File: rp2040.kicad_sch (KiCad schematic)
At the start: 25 parts, among them J1 Conn_01x06, J10 Conn_01x02, U6 RP2040, Y1 12.0MHz

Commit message: TT 4+ pre-route alpha schem and layout reset
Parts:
- C? (x2): footprint Capacitor_SMD:C_0402_1005Metric -> Capacitor_SMD:C_0603_1608Metric; MPN 1uF 0402 -> 1uF 0603
- C?: JLC C85864 -> (none); MPN CL10B104KB8NNND -> 100n 10% 25V XR 0603
- R11: footprint Resistor_SMD:R_0402_1005Metric -> Resistor_SMD:R_0603_1608Metric; MPN 10k 0402 -> 10k 0603

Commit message: reassignments, new dual-purpose pmod/iohead, floorplan
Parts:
- C?: footprint Capacitor_SMD:C_0603_1608Metric -> Capacitor_SMD:C_0402_1005Metric
- J1: footprint Connector_PinHeader_2.54mm:PinHeader_1x06_P2.54mm_Vertical -> Connector_PinHeader_2.54mm:PinHeader_1x06_P2.54mm_Vertical_SMD_Pin1Right
- R11, R? (x6): footprint Resistor_SMD:R_0603_1608Metric -> Resistor_SMD:R_0402_1005Metric
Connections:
- net +3.3V is gone; now on net QSPI_SD1: J1.5 (Pin_5)
- net BOOT_MODE: now also J1.2 (Pin_2); no longer J1.1 (Pin_1)
- net QSPI_CLK: now also J1.3 (Pin_3); no longer J1.2 (Pin_2)
- net QSPI_SD0: now also J1.4 (Pin_4); no longer J1.3 (Pin_3)
- net QSPI_SD1: no longer J1.4 (Pin_4)
- new net +3V3: J1.1 (Pin_1)
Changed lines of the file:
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@@
     (stroke (width 0) (type default))
   )
-  (wire (pts (xy 25.4 78.74) (xy 30.48 78.74))
+  (wire (pts (xy 25.4 78.74) (xy 35.56 78.74))
     (stroke (width 0) (type default))
   )
@@
     (effects (font (size 1 1)) (justify left bottom))
   )
-  (label "QSPI_SS" (at 35.56 68.58 180) (fields_autoplaced)
+  (label "QSPI_SS" (at 35.56 71.12 180) (fields_autoplaced)
     (effects (font (size 1.27 1.27)) (justify right bottom))
   )
@@
     (effects (font (size 1.27 1.27)) (justify right bottom))
   )
-  (label "QSPI_SD1" (at 35.56 76.2 180) (fields_autoplaced)
+  (label "QSPI_SD1" (at 35.56 78.74 180) (fields_autoplaced)
     (effects (font (size 1.27 1.27)) (justify right bottom))
   )
@@
     (effects (font (size 1.27 1.27)) (justify left bottom))
   )
-  (label "QSPI_SD0" (at 35.56 73.66 180) (fields_autoplaced)
+  (label "QSPI_SD0" (at 35.56 76.2 180) (fields_autoplaced)
     (effects (font (size 1.27 1.27)) (justify right bottom))
   )
@@
     (effects (font (size 1.27 1.27)) (justify right bottom))
   )
-  (label "QSPI_CLK" (at 35.56 71.12 180) (fields_autoplaced)
+  (label "QSPI_CLK" (at 35.56 73.66 180) (fields_autoplaced)
     (effects (font (size 1.27 1.27)) (justify right bottom))
   )
@@
       (effects (font (size 1.27 1.27)) (justify left))
     )
-    (property "Footprint" "Resistor_SMD:R_0603_1608Metric" (at 80.01 167.64 0)
+    (property "Footprint" "Resistor_SMD:R_0402_1005Metric" (at 80.01 167.64 0)
       (effects (font (size 1.27 1.27)) hide)
     )
@@
       (effects (font (size 1.27 1.27)) (justify left))
     )
-    (property "Footprint" "Resistor_SMD:R_0603_1608Metric" (at 73.66 109.22 0)
+    (property "Footprint" "Resistor_SMD:R_0402_1005Metric" (at 73.66 109.22 0)
       (effects (font (size 1.27 1.27)) hide)
     )
@@
       (effects (font (size 1.27 1.27)) (justify left))
     )
-    (property "Footprint" "Resistor_SMD:R_0603_1608Metric" (at 25.4 170.18 0)
+    (property "Footprint" "Resistor_SMD:R_0402_1005Metric" (at 25.4 170.18 0)
       (effects (font (size 1.27 1.27)) hide)
     )
@@
       (effects (font (size 1.27 1.27)) hide)
     )
-    (property "Footprint" "Connector_PinHeader_2.54mm:PinHeader_1x06_P2.54mm_Vertical" (at 20.32 73.66 0)
+    (property "Footprint" "Connector_PinHeader_2.54mm:PinHeader_1x06_P2.54mm_Vertical_SMD_Pin1Right" (at 20.32 73.66 0)
       (effects (font (size 1.27 1.27)) hide)
     )
@@
       (effects (font (size 1.27 1.27)) (justify right))
     )
-    (property "Footprint" "Resistor_SMD:R_0603_1608Metric" (at 73.66 48.26 0)
+    (property "Footprint" "Resistor_SMD:R_0402_1005Metric" (at 73.66 48.26 0)
       (effects (font (size 1.27 1.27)) hide)
     )
@@
       (effects (font (size 1.27 1.27)) (justify left))
     )
-    (property "Footprint" "Resistor_SMD:R_0603_1608Metric" (at 73.66 167.64 0)
+    (property "Footprint" "Resistor_SMD:R_0402_1005Metric" (at 73.66 167.64 0)
       (effects (font (size 1.27 1.27)) hide)
     )
@@
     )
   )
-  (symbol (lib_id "power:+3.3V") (at 30.48 78.74 270) (mirror x) (unit 1)
+  (symbol (lib_id "power:+3V3") (at 35.56 68.58 270) (mirror x) (unit 1)
     (in_bom yes) (on_board yes) (dnp no) (fields_autoplaced)
-    (property "Reference" "#PWR09" (at 26.67 78.74 0)
+    (property "Reference" "#PWR09" (at 31.75 68.58 0)
       (effects (font (size 1.27 1.27)) hide)
     )
-    (property "Value" "+3.3V" (at 33.655 78.74 90)
+    (property "Value" "+3V3" (at 38.735 68.58 90)
       (effects (font (size 1.27 1.27)) (justify left))
     )
-    (property "Footprint" "" (at 30.48 78.74 0)
+    (property "Footprint" "" (at 35.56 68.58 0)
       (effects (font (size 1.27 1.27)) hide)
     )
-    (property "Datasheet" "" (at 30.48 78.74 0)
+    (property "Datasheet" "" (at 35.56 68.58 0)
       (effects (font (size 1.27 1.27)) hide)
     )
@@
       (effects (font (size 1.27 1.27)) (justify left))
     )
-    (property "Footprint" "Resistor_SMD:R_0603_1608Metric" (at 86.36 167.64 0)
+    (property "Footprint" "Resistor_SMD:R_0402_1005Metric" (at 86.36 167.64 0)
       (effects (font (size 1.27 1.27)) hide)
     )
@@
       (effects (font (size 1.27 1.27)))
     )
-    (property "Footprint" "Capacitor_SMD:C_0603_1608Metric" (at 57.15 167.64 0)
+    (property "Footprint" "Capacitor_SMD:C_0402_1005Metric" (at 57.15 167.64 0)
       (effects (font (size 1.27 1.27)) hide)
     )
@@
       (effects (font (size 1.27 1.27)) (justify left))
     )
-    (property "Footprint" "Resistor_SMD:R_0603_1608Metric" (at 67.31 167.64 0)
+    (property "Footprint" "Resistor_SMD:R_0402_1005Metric" (at 67.31 167.64 0)
       (effects (font (size 1.27 1.27)) hide)
     )

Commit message: TT04 new breakout pre-rework
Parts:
- C?: Characteristics (none) -> 6pF 10% 50V XR 0402; MPN 6pF 10% 50V XR 0402 -> CC0402BRNPO9BN6R0
- C? (x8): Characteristics (none) -> 100n 10% 25V XR 0402; MPN 100nF 0402 -> CL05A104KA5NNNC; MPN_ALT (none) -> GRM155R71E104KE14J
- C? (x2): Characteristics (none) -> 1u 10V XR 0603; MPN 1uF 0603 -> CL10A105KA8NNNC; MPN_ALT (none) -> C0603C105K4RAC7411
- C?: Characteristics (none) -> 6pF 10% 50V XR 0402; MPN 6pF 10% 50V XR 0402 -> CC0402BRNPO9BN6R0; MPN_ALT (none) -> 0402N6R0D500CT
- C?: Characteristics (none) -> 100n 10% 25V XR 0402; MPN 100n 10% 25V XR 0603 -> CL05A104KA5NNNC; MPN_ALT (none) -> GRM155R71E104KE14J
- R11: Characteristics (none) -> 10k 0402; MPN 10k 0603 -> RC0402FR-0710KL; MPN_ALT (none) -> WR04X1002FTL
- R? (x5): Characteristics (none) -> 10k 0402; MPN (none) -> RC0402FR-0710KL; MPN_ALT (none) -> WR04X1002FTL
- R?: Characteristics (none) -> 1k 0402; MPN (none) -> CR0402-FX-1001GLF; MPN_ALT (none) -> WR04X1001FTL
- U6: DigikeyPN (none) -> 2648-SC0914(13)CT-ND; MPN (none) -> SC0914(13)
- U?: DigikeyPN (none) -> W25Q32JVSSIQ-ND
- Y1: DigikeyPN (none) -> 1923-830108206909DKR-ND

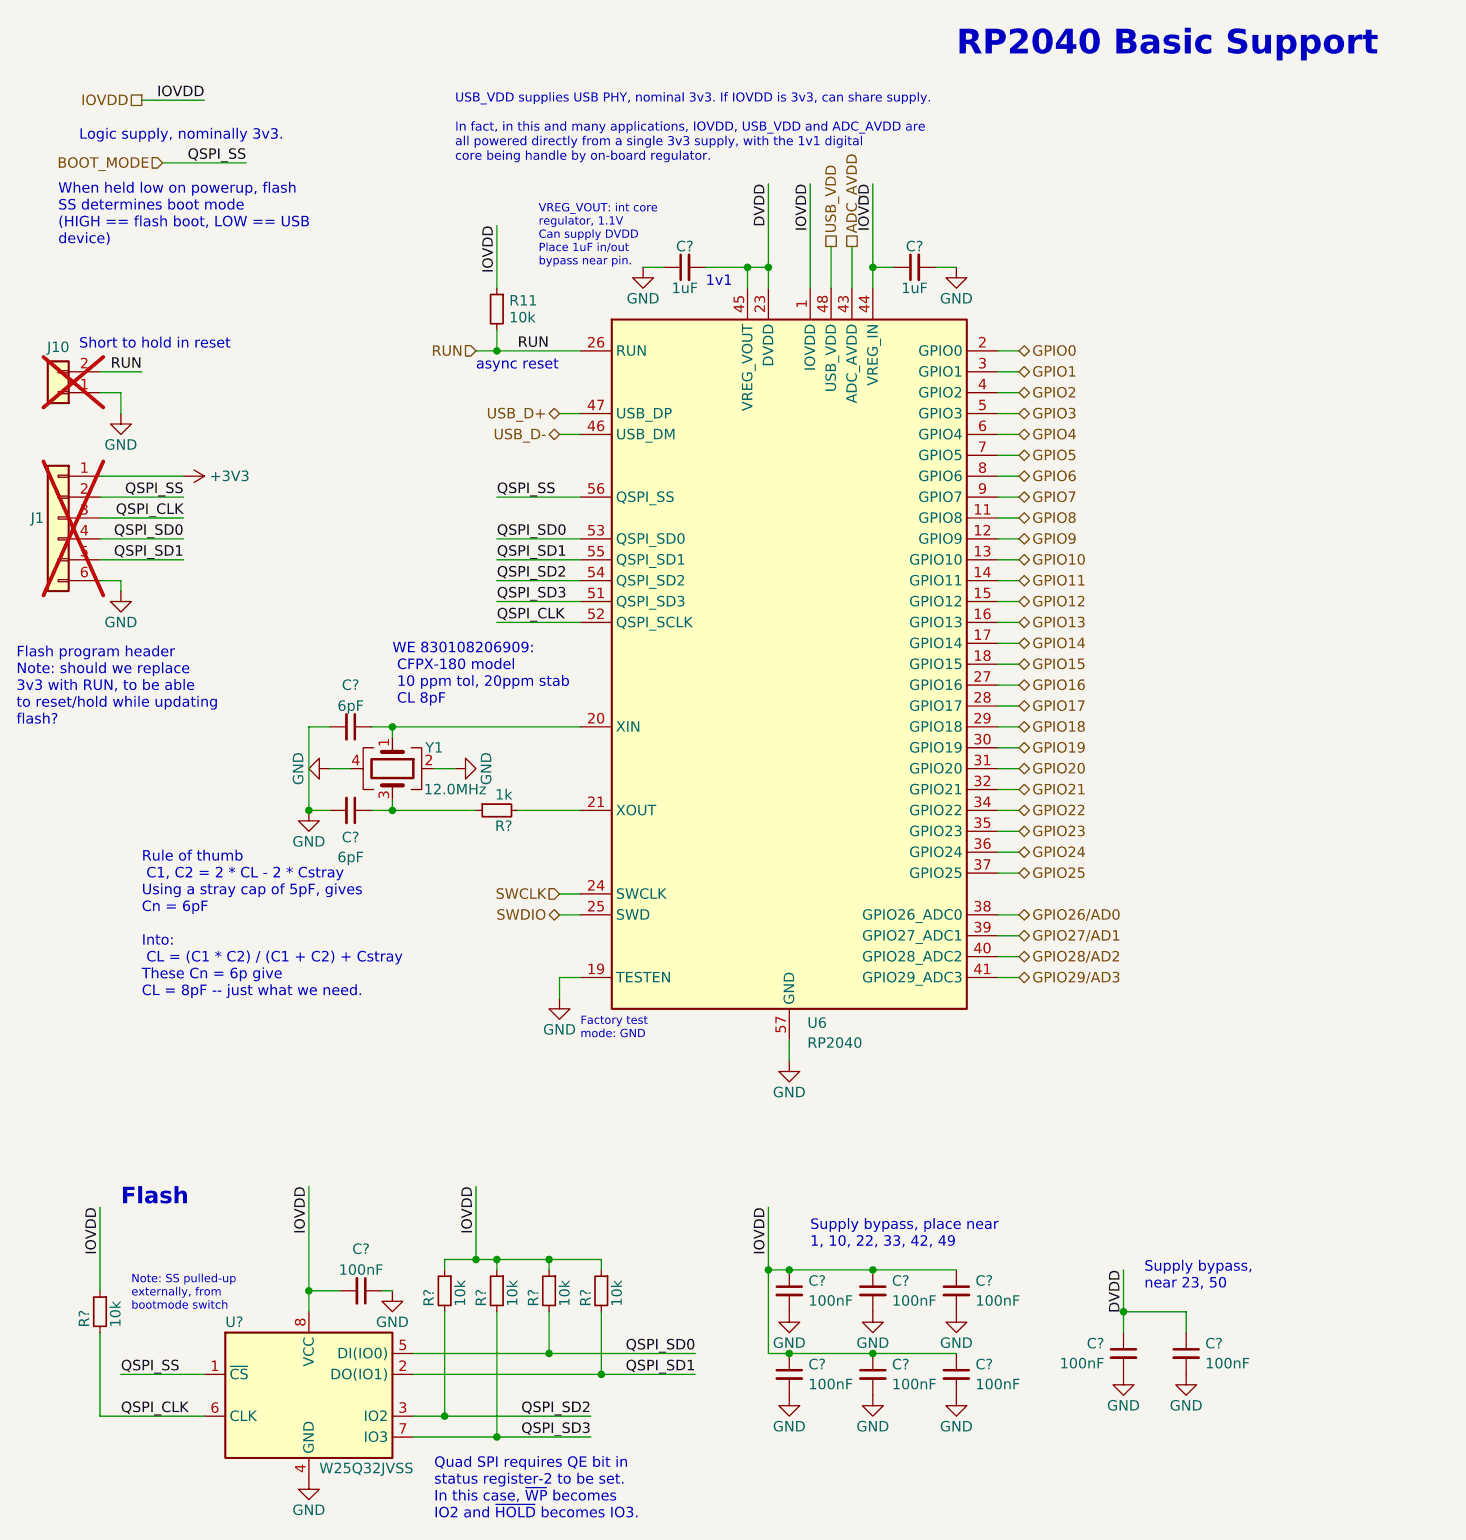
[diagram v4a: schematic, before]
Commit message: v1.0.4 alpha as assembled for test run
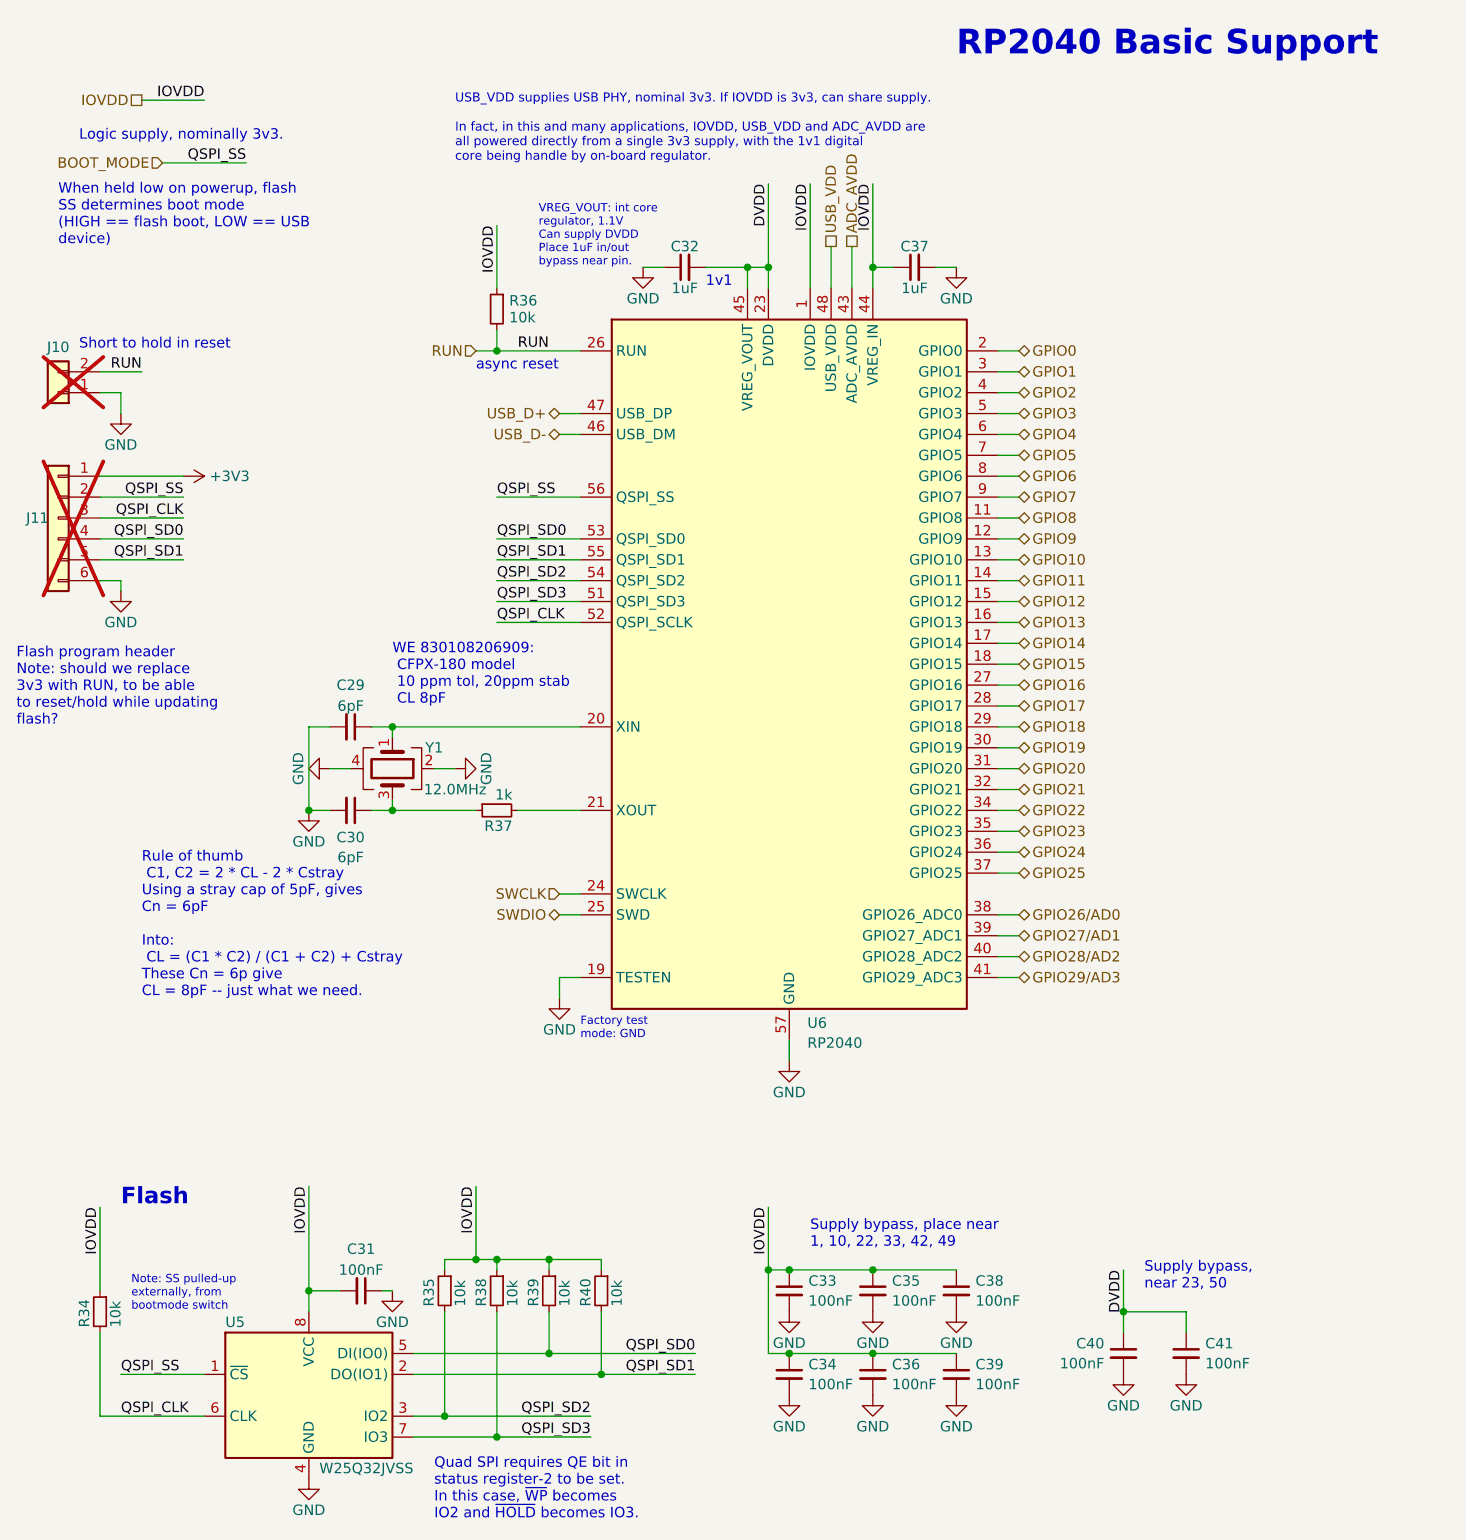
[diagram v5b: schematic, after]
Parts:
- gave numbers to parts that had none: 20
- renumbered J1 to J11, R11 to R36

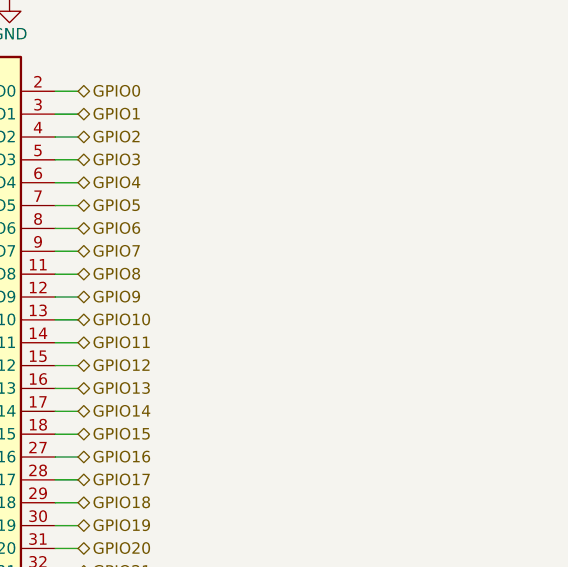
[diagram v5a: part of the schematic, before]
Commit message: reworked UART pmod, 1v8 fused and instrumentable
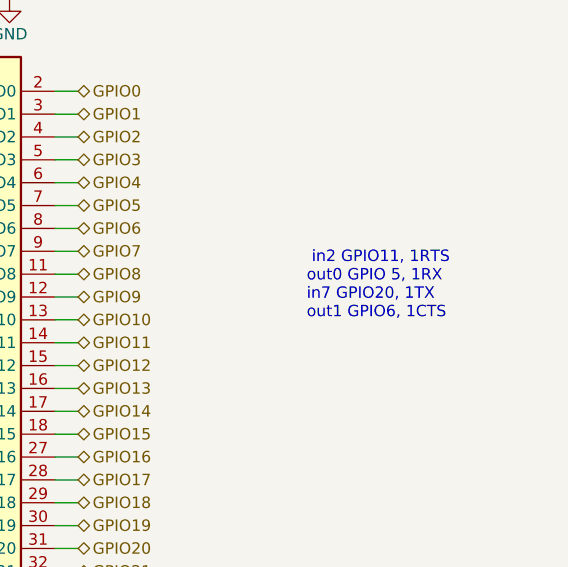
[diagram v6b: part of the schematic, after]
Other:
- note added: "in2 GPIO11, 1RTS out0 GPIO 5, 1RX in7 GPIO20, 1TX out1 GPIO6, 1CTS"
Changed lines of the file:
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@@
+    (effects (font (size 1.27 1.27)) (justify left bottom))
+  )
+  (text " in2 GPIO11, 1RTS\nout0 GPIO 5, 1RX \nin7 GPIO20, 1TX\nout1 GPIO6, 1CTS"
+    (at 162.56 78.74 0)
     (effects (font (size 1.27 1.27)) (justify left bottom))
   )
